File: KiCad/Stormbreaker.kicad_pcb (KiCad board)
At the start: 4 copper layers, 50.2 x 21 mm, 50 parts, among them J1 Micro_SD_Card_Det2, J2 USB_C_Receptacle_USB2.0_14P, J3 PROG, J5 I2C, Q1 PMOS, Q2 NMOS, SW1 SW_Push, U1 BQ25895RTW, U3 ATtiny1616-M, U4 HUSB238A

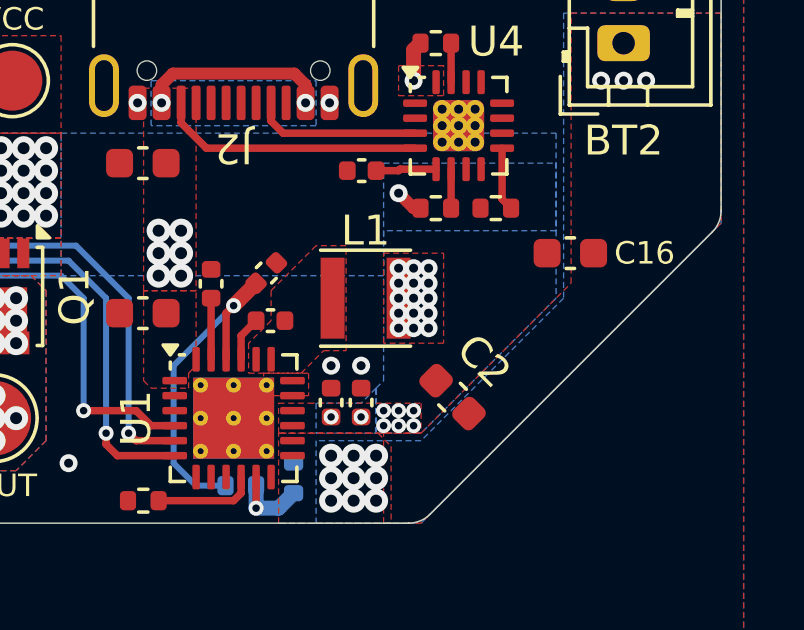
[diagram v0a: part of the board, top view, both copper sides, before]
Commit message: Switch to larger inductor
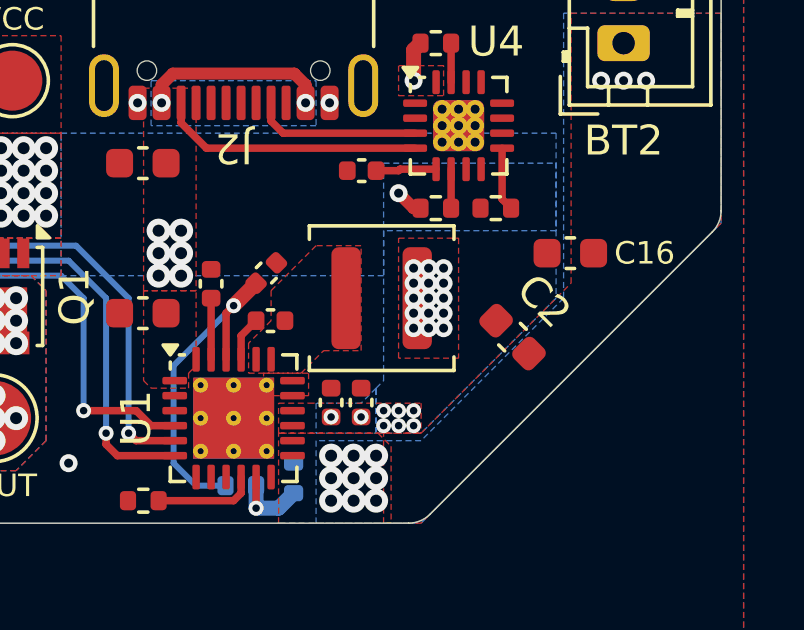
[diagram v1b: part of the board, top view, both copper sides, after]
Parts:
- L1: value 1uH -> 3.3uH; footprint Inductor_SMD:L_Taiyo-Yuden_MD-3030 -> Inductor_SMD:L_Coilcraft_XAL4040-XXX
- moved C2 2.83 mm to (157.3, 55.8)
- moved L1 0.53 mm to (152.9, 54.5)
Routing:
- net GND: vias 36 -> 34

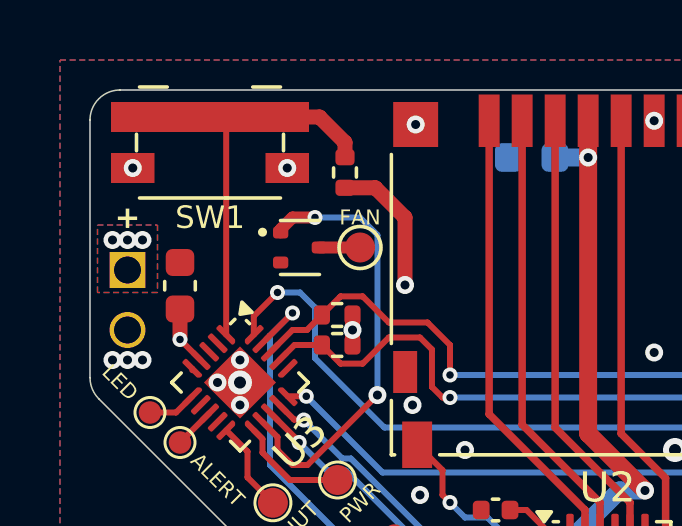
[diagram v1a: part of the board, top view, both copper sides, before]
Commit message: Switch to different button
Something's up with KiCad, not sure why.
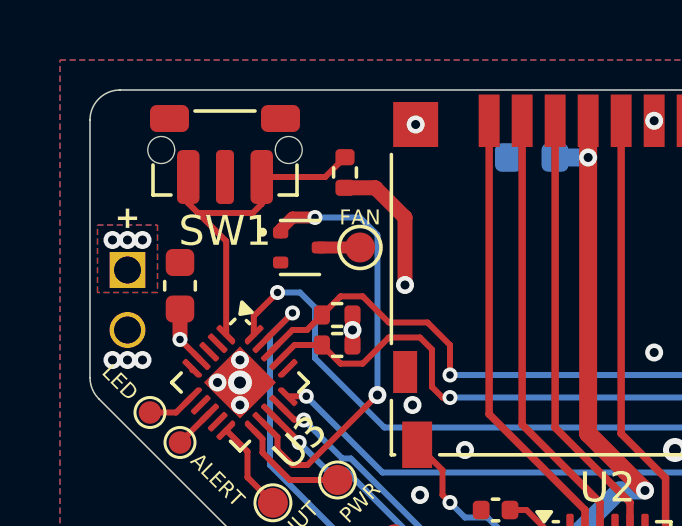
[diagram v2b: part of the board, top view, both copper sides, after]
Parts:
- SW1: footprint Button_Switch_SMD:Panasonic_EVQPUK_EVQPUB -> Button_Switch_SMD:SW_Push_1P1T-MP_NO_Horizontal_Alps_SKRTLAE010
- moved SW1 0.56 mm to (118.5, 43.0), turned to 180 degrees
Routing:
- net /PowerButton: track 15.3 -> 12.0 mm
- net GND: vias 34 -> 32

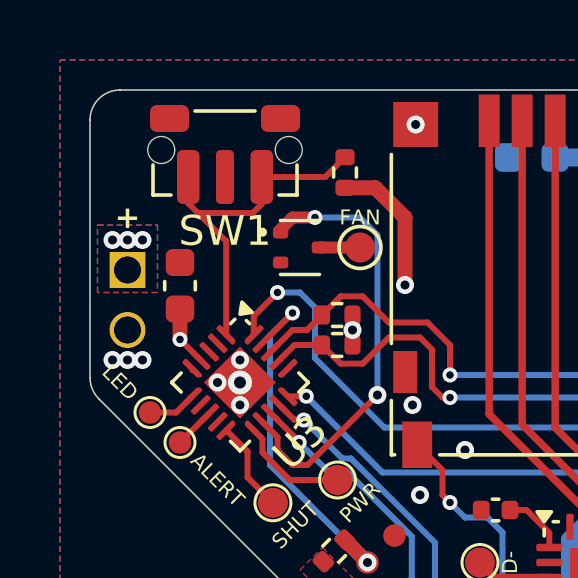
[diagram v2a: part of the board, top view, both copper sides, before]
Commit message: WIP -- Move to PlatformIO
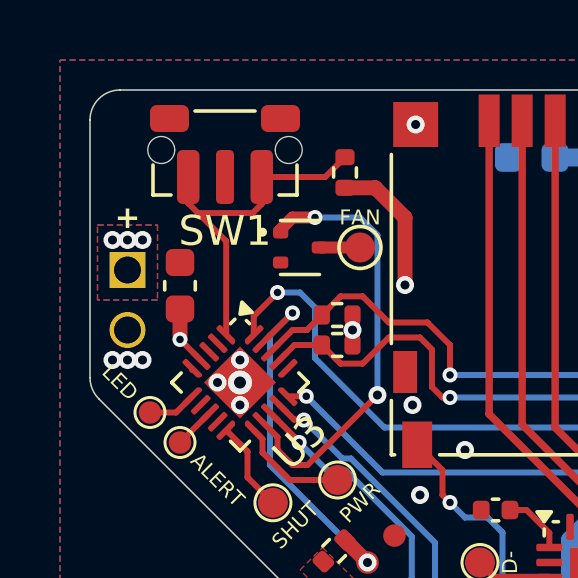
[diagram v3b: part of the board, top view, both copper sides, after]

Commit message: Nearing completion of firmware rewrite
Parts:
- L1: footprint Inductor_SMD:L_Coilcraft_XAL4040-XXX -> Stormbreaker:L_PCMB053T
- moved C2 4.48 mm to (159.2, 51.8), turned to 180 degrees
- moved R11 1.59 mm to (154.2, 44.5), turned to 90 degrees
- moved R12 1.35 mm to (157.2, 50.2)
- moved R6 1.35 mm to (155.2, 50.3)
- moved U4 1.35 mm to (156.0, 47.5)
- moved L1 1.05 mm to (153.9, 54.2)
- moved C15 0.98 mm to (153.2, 50.2)
- moved C16 0.25 mm to (159.2, 53.2)
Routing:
- net Net-(U4-GATE): track 1.30 -> 2.70 mm
- net CC1: track 5.57 -> 6.68 mm
- net CC2: track 8.81 -> 9.80 mm
- net VCC: vias 43 -> 37

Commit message: Several misc PCB improvements
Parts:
- R2, R3: moved to F.Cu
- TP11: value ALERT -> ~{ALERT}
- moved R3 8.00 mm to (148.5, 52.8), turned to -135 degrees
- moved R2 7.04 mm to (143.0, 61.2), turned to 0 degrees
- moved R1 2.23 mm to (143.0, 60.2)
- moved C7 0.48 mm to (147.2, 54.5)
- moved R11 0.25 mm to (154.0, 44.5)
- moved L1 0.20 mm to (153.8, 54.2)
- moved C4 0.13 mm to (149.0, 53.8)
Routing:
- net Net-(U1-TS): track 3.24 -> 18.4 mm, vias 1 -> 2
- net Net-(U1-REGN): track 11.1 -> 4.02 mm, vias 1 -> 0
- net Net-(U1-ILIM): track 3.39 -> 5.80 mm
- net VBUS: track 16.5 -> 18.2 mm, vias 10 -> 9
- net VCC: vias 37 -> 33
- net GND: vias 32 -> 31

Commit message: Misc board improvements
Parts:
- removed C11: 4.7μF, Capacitor_SMD:C_0603_1608Metric
- TP11: value ~{ALERT} -> ALERT
- moved J2 0.06 mm to (148.0, 44.2)
- moved Q1 0.06 mm to (140.0, 54.5)
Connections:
- U1 pad 4: /BQ_STAT -> unconnected-(U1-STAT-Pad4)
- U1 pad 7: unconnected-(U1-INT-Pad7) -> /BQ_~{INT}
- U3 pad 15: /BQ_STAT -> /BQ_~{INT}
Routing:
- net /BQ_~{INT}: track 0.00 -> 32.8 mm, vias 0 -> 2
- net /BQ_STAT: track 30.8 -> 0.00 mm, vias 2 -> 0
- net SD_VCC: track 22.5 -> 21.4 mm, vias 3 -> 2

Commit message: v3 hardware design: largely complete
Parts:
- removed R12: 6.04k, Resistor_SMD:R_0402_1005Metric
- added TP9: GND, TestPoint:TestPoint_Pad_D2.5mm, F.Cu at (136.8, 60.2)
- C12: footprint Capacitor_SMD:C_0603_1608Metric -> Capacitor_SMD:C_0402_1005Metric
- SW1: footprint Button_Switch_SMD:SW_Push_1P1T-MP_NO_Horizontal_Alps_SKRTLAE010 -> Stormbreaker:SW_TL3330AF260QG
- TP10, TP11: footprint Stormbreaker:TestPoint_Pad_D0.75mm_Small -> Stormbreaker:TestPoint_Pad_D1.0mm_Small
- TP4: footprint TestPoint:TestPoint_Pad_D1.0mm -> Stormbreaker:TestPoint_Pad_D1.0mm_Small
- moved TP4 14.6 mm to (121.0, 60.8), turned to 135 degrees
- moved Q2 12.7 mm to (123.0, 58.8), turned to -135 degrees
- moved J5 9.39 mm to (133.0, 61.8), turned to 90 degrees
- moved TP2 6.40 mm to (123.0, 61.8), turned to 135 degrees
- moved TP6 5.93 mm to (119.5, 59.2), turned to 135 degrees
- moved R5 4.96 mm to (118.8, 47.0), turned to 0 degrees
- moved TP1 4.25 mm to (124.5, 61.8), turned to 135 degrees
- moved TP7 3.65 mm to (118.0, 57.8), turned to 135 degrees
- moved TP11 3.54 mm to (116.5, 56.2), turned to -45 degrees
- moved TP10 3.16 mm to (115.0, 54.8), turned to -45 degrees
- moved R7 1.24 mm to (121.2, 55.5)
- moved J3 1.06 mm to (122.5, 56.0)
- moved R6 1.01 mm to (156.2, 50.3), turned to 180 degrees
- moved C15 1.00 mm to (154.2, 50.3)
- moved R1 0.79 mm to (143.8, 60.5)
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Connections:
- R6 pad 1: VBUS -> GND
- U4 pad 10: unconnected-(U4-SCL-Pad10) -> SCL_2
- U4 pad 8: unconnected-(U4-ADDR-Pad8) -> GND
- U4 pad 9: Net-(U4-SDA) -> SDA_2
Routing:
- net SCL_2: track 34.7 -> 61.0 mm
- net SDA_2: track 34.5 -> 59.2 mm
- net SCL: track 9.82 -> 19.5 mm
- net SDA: track 10.4 -> 17.8 mm
- net D-: track 2.52 -> 8.95 mm
- net /PowerButton: track 12.0 -> 6.10 mm
- net D+: track 2.55 -> 8.18 mm
- net VBUS: track 18.2 -> 12.7 mm, vias 9 -> 6
- net FAN_PWM: track 14.7 -> 10.1 mm, vias 2 -> 0
- net /ALERT: track 1.38 -> 5.09 mm
- net /Wii_POWER: track 3.74 -> 7.34 mm
- net /LED: track 1.63 -> 5.05 mm
- net /Wii_SHUTDOWN: track 3.06 -> 5.63 mm
- net Net-(U4-SDA): track 2.12 -> 0.00 mm
- net VCC: track 10.5 -> 8.51 mm, vias 33 -> 42
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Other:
- board size 50.2 x 21 mm -> 50.2 x 21.5 mm
- board text added: "SCL"
- board text added: "SDA"
- board text removed: "GND"

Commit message: Nearing completion of revision 3
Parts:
- moved TP8 0.25 mm to (141.0, 47.8)
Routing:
- net /PA0: track 11.7 -> 10.8 mm
- net VCC: vias 42 -> 57
- net VBUS: vias 6 -> 10
- net GND: vias 37 -> 41
- net /BATT: vias 15 -> 19
